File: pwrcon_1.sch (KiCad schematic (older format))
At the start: 32 parts, among them J1 Conn_01x02, J4 CON3, J5 Conn_01x03_Female, J6 Conn_02x04_Odd_Even, J7 Conn_01x03_Female, Q1 Q_PNP_BCE, U1 LM358

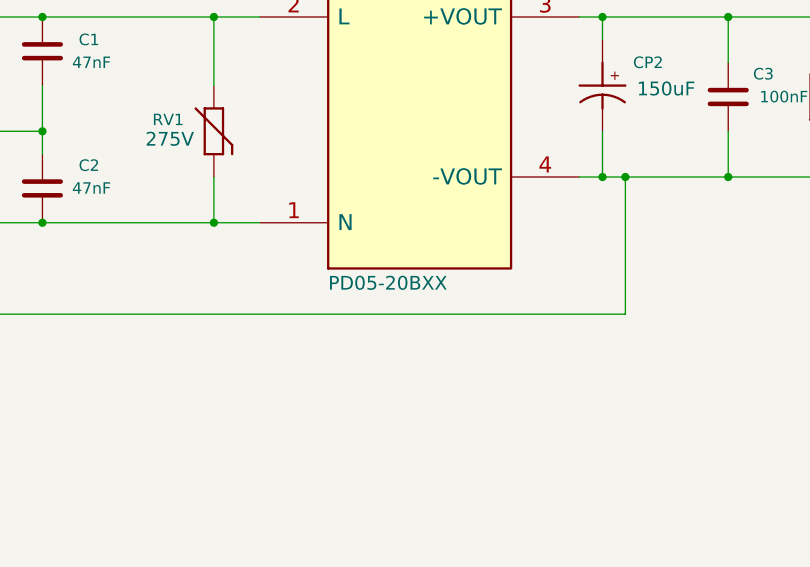
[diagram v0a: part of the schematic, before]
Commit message: Changed pcb file for transistor flip in previous commit. Changed PSU module name in schematic
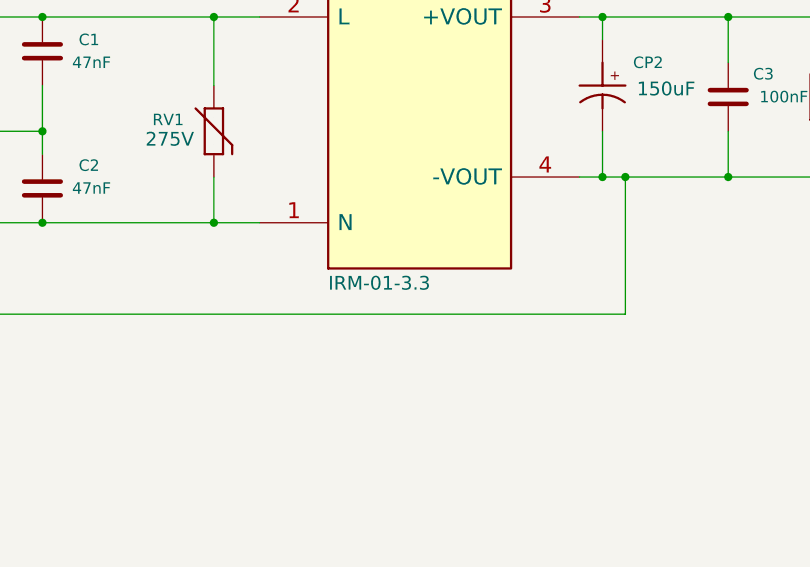
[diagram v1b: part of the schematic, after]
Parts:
- PSU1: value PD05-20BXX -> IRM-01-3.3; Manufacturer PowerPax -> Meanwell; PartNo PD05-20BXX -> IRM-01-3.3
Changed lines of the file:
@@
 EESchema Schematic File Version 4
-LIBS:pwrcon_1-cache
-EELAYER 29 0
+EELAYER 30 0
 EELAYER END
 $Descr A4 11693 8268
@@
 P 7400 1350
 F 0 "PSU1" H 7500 1400 50  0000 C CNN
-F 1 "PD05-20BXX" H 7400 -50 60  0000 L BNN
+F 1 "IRM-01-3.3" H 7400 -50 60  0000 L BNN
 F 2 "pwrcon:Meanwell_IRM_01_fixed" H 7400 -20 60  0001 C CNN
 F 3 "" H 7400 -20 60  0000 C CNN
 F 4 "Y" H 7400 1350 50  0001 C CNN "Fit"
-F 5 "PowerPax" H 7400 1350 50  0001 C CNN "Manufacturer"
-F 6 "PD05-20BXX" H 7400 1350 50  0001 C CNN "PartNo"
+F 5 "Meanwell" H 7400 1350 50  0001 C CNN "Manufacturer"
+F 6 "IRM-01-3.3" H 7400 1350 50  0001 C CNN "PartNo"
 	1    7400 1350
 	1    0    0    -1

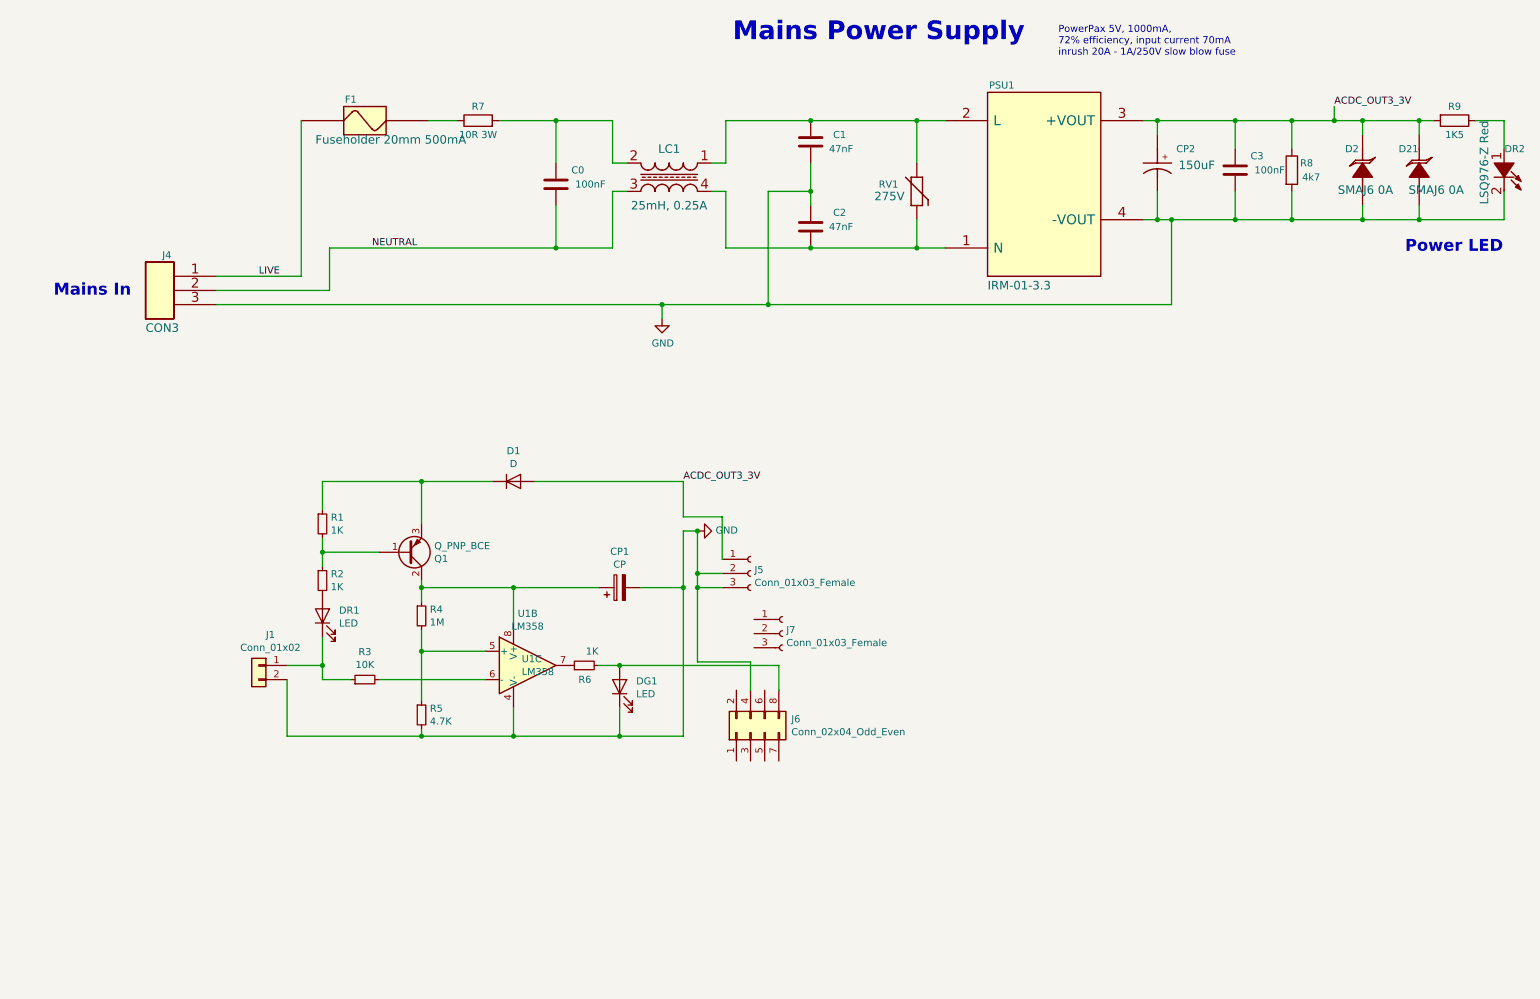
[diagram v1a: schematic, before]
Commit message: Changed module to 5V, added 3V3 regulator and isolated RS485 transceiver, changed to SMD
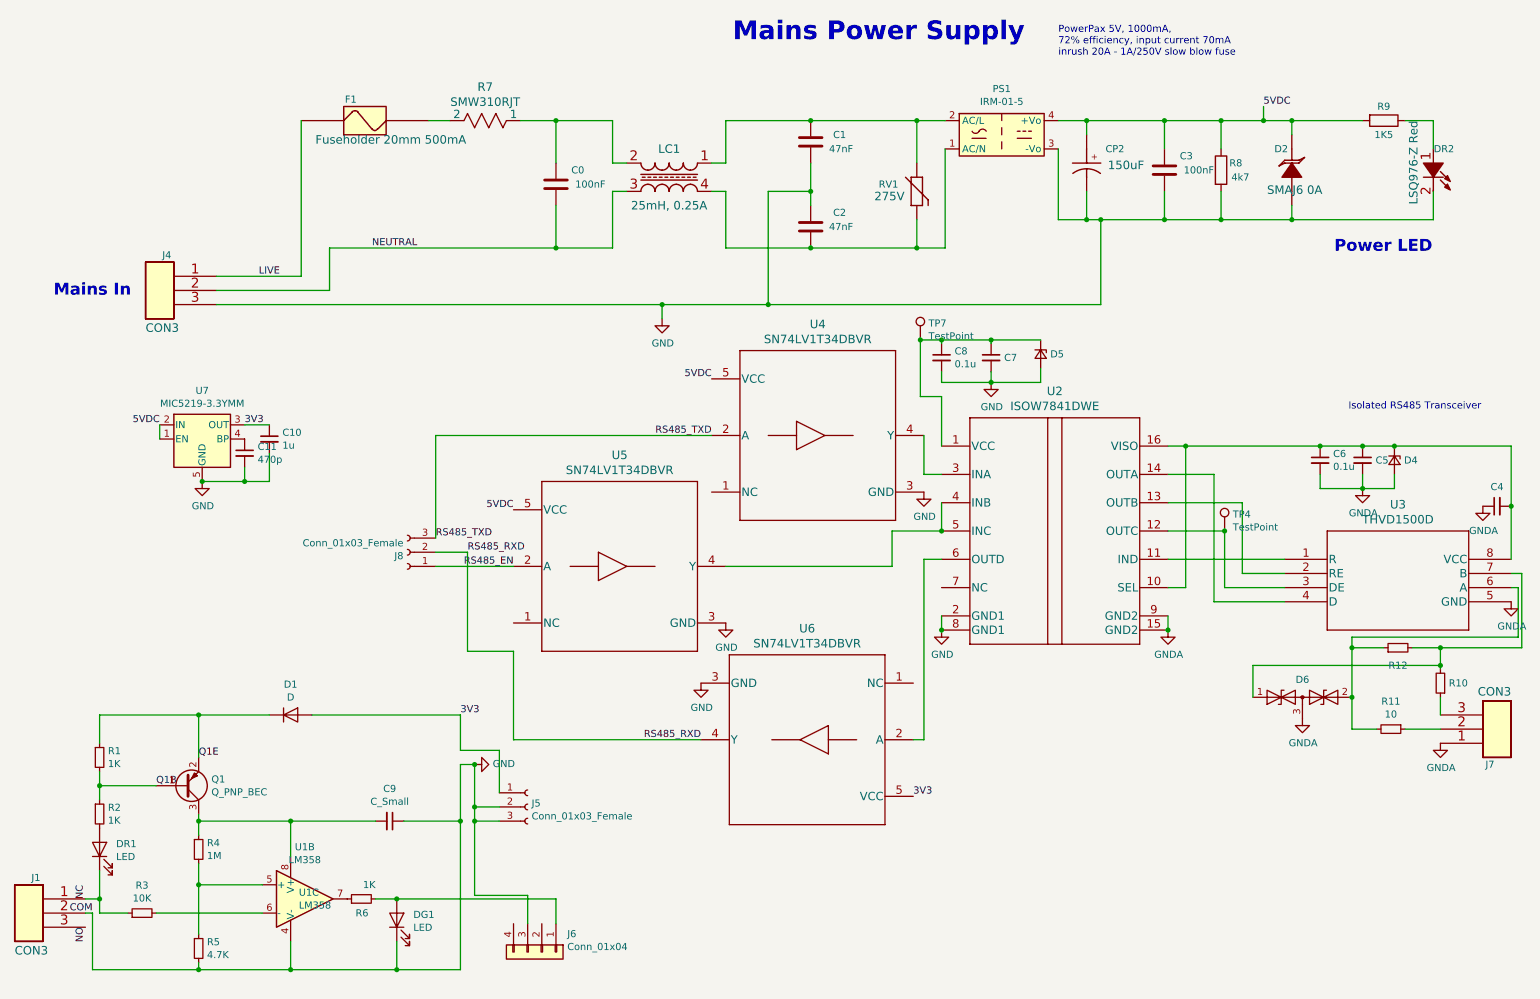
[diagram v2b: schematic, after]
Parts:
- removed CP1: CP, Capacitor_THT:CP_Radial_D8.0mm_P5.00mm, symbol Device:CP
- removed D21: SMAJ6 0A, Diode_SMD:D_SMB_Handsoldering, symbol pwrcon-rescue:DIODE_TVS-baseunit
- removed J1: Conn_01x02, Connector_Wire:SolderWirePad_1x02_P5.08mm_Drill1.5mm, symbol Connector_Generic:Conn_01x02
- removed J6: Conn_02x04_Odd_Even, Connector_PinSocket_2.54mm:PinSocket_2x04_P2.54mm_Vertical, symbol Connector_Generic:Conn_02x04_Odd_Even
- removed J7: Conn_01x03_Female, pwrcon:SolderWirePad_1x03_P2.54mm_Drill0.8mm, symbol Connector:Conn_01x03_Female
- removed PSU1: IRM-01-3.3, pwrcon:Meanwell_IRM_01_fixed, symbol pwrcon-rescue:STM32F302K_QFPN32_4-baseunit
- removed Q1: Q_PNP_BCE, pwrcon:TO-92_BC237_307, symbol Device:Q_PNP_BCE
- removed R7: 10R 3W, Resistor_THT:R_Axial_DIN0207_L6.3mm_D2.5mm_P7.62mm_Horizontal, symbol Device:R
- added C10: 1u, Capacitor_SMD:C_0603_1608Metric_Pad1.05x0.95mm_HandSolder, symbol Device:C_Small
- added C11: 470p, Capacitor_SMD:C_0603_1608Metric_Pad1.05x0.95mm_HandSolder, symbol Device:C_Small
- added C4, C6, C8: 0.1u, Capacitor_SMD:C_0603_1608Metric_Pad1.05x0.95mm_HandSolder, symbol Device:C_Small
- added C5, C7: 10u, Capacitor_SMD:C_0603_1608Metric_Pad1.05x0.95mm_HandSolder, symbol Device:C_Small
- added C9: C_Small, Capacitor_SMD:C_0603_1608Metric_Pad1.05x0.95mm_HandSolder, symbol Device:C_Small
- added D4, D5: D_Zener_Small, Diode_SMD:D_SMB_Handsoldering, symbol Device:D_Zener_Small
- added D6: CDSOT23-SM712, Package_TO_SOT_SMD:SOT-23, symbol Device:D_TVS_x2_AAC
- added J1, J7: CON3, Connector_Phoenix_MC_HighVoltage:PhoenixContact_MCV_1,5_3-G-5.08_1x03_P5.08mm_Vertical, symbol pwrcon-rescue:CON3-baseunit
- added J6: Conn_01x04, Connector_PinSocket_2.54mm:PinSocket_1x04_P2.54mm_Vertical, symbol Connector_Generic:Conn_01x04
- added J8: Conn_01x03_Female, Connector_PinSocket_2.54mm:PinSocket_1x03_P2.54mm_Vertical, symbol Connector:Conn_01x03_Female
- added PS1: IRM-01-5, Converter_ACDC:Converter_ACDC_MeanWell_IRM-02-xx_THT, symbol Converter_ACDC:IRM-02-5
- added Q1: Q_PNP_BEC, Package_TO_SOT_SMD:SOT-23_Handsoldering, symbol Device:Q_PNP_BEC
- added R10, R11: 10, Resistor_SMD:R_0603_1608Metric_Pad1.05x0.95mm_HandSolder, symbol Device:R_Small
- added R12: 120, Resistor_SMD:R_0603_1608Metric_Pad1.05x0.95mm_HandSolder, symbol Device:R_Small
- added R7: SMW310RJT, SMW310RJT:SMW310RJT, symbol 2020-09-15_11-05-09:SMW310RJT
- added TP4, TP7: TestPoint, TestPoint:TestPoint_Loop_D2.50mm_Drill1.0mm, symbol Connector:TestPoint
- added U2: ISOW7841DWE, ISOW7841DWE:ISOW7841DWE, symbol 2020-09-12_17-09-47:ISOW7841DWE
- added U3: THVD1500D, THVD1500D:THVD1500D, symbol 2020-09-12_17-01-44:THVD1500D
- added U4, U5, U6: SN74LV1T34DBVR, SN74LV1T34DBVR:SN74LV1T34DBVR, symbol 2020-09-12_16-45-05:SN74LV1T34DBVR
- added U7: MIC5219-3.3YMM, Package_SO:MSOP-8_3x3mm_P0.65mm, symbol Regulator_Linear:MIC5219-3.3YMM
- C3: footprint Capacitor_THT:CP_Radial_D8.0mm_P5.00mm -> Capacitor_SMD:C_0603_1608Metric_Pad1.05x0.95mm_HandSolder; MFG Name (none) -> Taiyo Yuden; MFG Part Num (none) -> EMK107B7104KAHT
- CP2: footprint Capacitor_THT:CP_Radial_Tantal_D9.0mm_P5.00mm -> Capacitor_Tantalum_SMD:CP_EIA-7343-20_Kemet-V_Pad2.25x2.55mm_HandSolder; Manufacturer AVX -> AVX / Kemet; PartNo TRJD157K010R0150 -> TRJD157K010R0150 / T495V157M010ATE150
- D1: footprint Diode_THT:D_A-405_P5.08mm_Vertical_AnodeUp -> Diode_SMD:D_SOD-123
- D2: footprint Diode_THT:D_DO-27_P5.08mm_Vertical_AnodeUp -> Diode_SMD:D_SMA; Manufacturer Multicomp -> Multicomp / Littelfuse
- DG1: footprint LED_THT:LED_D1.8mm_W3.3mm_H2.4mm -> LED_SMD:LED_0603_1608Metric_Pad1.05x0.95mm_HandSolder; MFG Name (none) -> Rohm; MFG Part Num (none) -> SML-D12M8WT86
- DR1: footprint LED_THT:LED_D1.8mm_W3.3mm_H2.4mm -> LED_SMD:LED_0603_1608Metric_Pad1.05x0.95mm_HandSolder; MFG Name (none) -> Rohm; MFG Part Num (none) -> SML-D12V8WT86
- DR2: footprint LED_THT:LED_D1.8mm_W3.3mm_H2.4mm -> LED_SMD:LED_0603_1608Metric_Pad1.05x0.95mm_HandSolder; PartNo LSQ976-Z -> LS Q976-NR-1
- R1, R2, R3, R4, R6, R9: footprint Resistor_THT:R_Axial_DIN0207_L6.3mm_D2.5mm_P7.62mm_Horizontal -> Resistor_SMD:R_0603_1608Metric
- R5, R8: footprint Resistor_THT:R_Axial_DIN0207_L6.3mm_D2.5mm_P7.62mm_Horizontal -> Resistor_SMD:R_0603_1608Metric_Pad1.05x0.95mm_HandSolder
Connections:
- net GND: now also C10.2, C11.2, C7.2, C8.2, C9.1, D5.2 (A), J1.2, J6.3 (Pin_3), PS1.3 (-Vo), U2.2 (GND1), U2.8 (GND1), U4.3 (GND), U5.3 (GND), U6.3 (GND), U7.5 (GND), U7.6 (GND), U7.7 (GND), U7.8 (GND)
- net at C2.1, LC1.4, RV1.2: now also PS1.1 (AC/N)
- net at C1.2, LC1.1, RV1.1: now also PS1.2 (AC/L)
- net at F1.2: now also R7.2
- net at C0.2, LC1.2: now also R7.1
- net Q1E: now reaches D1.1 (K), R1.1
- net Q1E: now also Q1.2 (E)
- net Q1B: now reaches R1.2, R2.1
- net Q1B: now also Q1.1 (B)
- net at R4.1, U1.8 (V+): now also C9.2, Q1.3 (C)
- net at DG1.2 (A), R6.2: now also J6.1 (Pin_1)
- net NC: now reaches DR1.1 (K), R3.1
- net NC: now also J1.1
- net ACDC_OUT3_3V renamed 5VDC
- net 5VDC: now also PS1.4 (+Vo), U4.5 (VCC), U5.5 (VCC), U7.1 (EN), U7.2 (IN); no longer D1.2 (A), J5.1 (Pin_1)
- new net: U2.11 (IND), U3.1 (R)
- new net: U2.13 (OUTB), U3.2 (RE)
- new net: TP4.1, U2.12 (OUTC), U3.3 (DE)
- new net: U2.14 (OUTA), U3.4 (D)
- new net: D6.2 (A2), R11.2, R12.1, U3.6 (A)
- new net: D6.1 (A1), R10.2, R12.2, U3.7 (B)
- new net: C4.2, C5.1, C6.1, D4.1 (K), U2.10 (SEL), U2.16 (VISO), U3.8 (VCC)
- new net: C7.1, C8.1, D5.1 (K), TP7.1, U2.1 (VCC)
- new net: U2.3 (INA), U4.4 (Y)
- new net: U2.4 (INB), U2.5 (INC), U5.4 (Y)
- new net: U2.6 (OUTD), U6.2 (A)
- new net: C11.1, U7.4 (BP)
- new net: J7.2, R11.1
- new net: J7.3, R10.1
- new net 3V3: C10.1, D1.2 (A), J5.1 (Pin_1), U6.5 (VCC), U7.3 (OUT)
- new net GNDA: C4.1, C5.2, C6.2, D4.2 (A), D6.3 (common), J7.1, U2.15 (GND2), U2.9 (GND2), U3.5 (GND)
- new net NO: J1.3
- new net RS485_EN: J8.1 (Pin_1), U5.2 (A)
- new net RS485_RXD: J8.2 (Pin_2), U6.4 (Y)
- new net RS485_TXD: J8.3 (Pin_3), U4.2 (A)
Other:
- note added: "Isolated RS485 Transceiver"
- moved on the sheet: C3, CP2, D1, D2, DG1, DR1, DR2, J5, R1, R2, R3, R4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

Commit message: Preliminary routing
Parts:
- removed TP7: TestPoint, TestPoint:TestPoint_Loop_D2.50mm_Drill1.0mm, symbol Connector:TestPoint
- TP4: footprint TestPoint:TestPoint_Loop_D2.50mm_Drill1.0mm -> TestPoint:TestPoint_Loop_D1.80mm_Drill1.0mm_Beaded
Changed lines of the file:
@@
 F 0 "TP4" H 9133 4568 50  0000 L CNN
 F 1 "TestPoint" H 9133 4477 50  0000 L CNN
-F 2 "TestPoint:TestPoint_Loop_D2.50mm_Drill1.0mm" H 9275 4450 50  0001 C CNN
+F 2 "TestPoint:TestPoint_Loop_D1.80mm_Drill1.0mm_Beaded" H 9275 4450 50  0001 C CNN
 F 3 "~" H 9275 4450 50  0001 C CNN
 	1    9075 4450
@@
 Connection ~ 7075 3100
 $Comp
-L Connector:TestPoint TP7
-U 1 1 5F780F34
-P 6925 3100
-F 0 "TP7" H 6983 3218 50  0000 L CNN
-F 1 "TestPoint" H 6983 3127 50  0000 L CNN
-F 2 "TestPoint:TestPoint_Loop_D2.50mm_Drill1.0mm" H 7125 3100 50  0001 C CNN
-F 3 "~" H 7125 3100 50  0001 C CNN
-	1    6925 3100
-	1    0    0    -1
-$EndComp
-Connection ~ 6925 3100
-$Comp
 L Device:C_Small C6
